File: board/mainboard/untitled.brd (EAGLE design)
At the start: 90 x 61 mm, 25 parts

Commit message: add catch sensor
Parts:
- added Q5: (no value), adafruit:SOT23
- added R11, R12: (no value), generic:SMD1608
- added X1: JST-XH-03-PIN-ROUND-PAD, Rembrandt Electronics - JST XH Connectors v1-0:JST-XH-03-PACKAGE-ROUND-PAD
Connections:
- new net CATCH_1: Q5.2, R12.2
- new net N$9: Q5.3, R11.2, X1.3
- net +3V3: now also Q5.1, R12.1
- net +5V: now also R11.1, X1.1
- net GND: now also X1.2
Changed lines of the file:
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@@
 <attribute name="VALUE" x="-45.25" y="-61.34" size="1.016" layer="27"/>
+</element>
+<element name="X1" library="Rembrandt Electronics - JST XH Connectors v1-0" package="JST-XH-03-PACKAGE-ROUND-PAD" value="JST-XH-03-PIN-ROUND-PAD" x="-38.1" y="-67.31" smashed="yes">
+<attribute name="NAME" x="-43.655" y="-69.35" size="1.016" layer="25" ratio="10" rot="R90"/>
+<attribute name="VALUE" x="-42.7025" y="-63.4175" size="1.016" layer="27" ratio="10"/>
+</element>
+<element name="Q5" library="adafruit" package="SOT23" value="" x="-43.18" y="-73.66" smashed="yes">
+<attribute name="NAME" x="-45.085" y="-71.755" size="1.27" layer="25"/>
+<attribute name="VALUE" x="-45.085" y="-76.835" size="1.27" layer="27"/>
+</element>
+<element name="R11" library="generic" package="SMD1608" value="" x="-40.64" y="-78.74" smashed="yes">
+<attribute name="NAME" x="-41.44" y="-78.09" size="1.016" layer="25"/>
+<attribute name="VALUE" x="-41.44" y="-80.39" size="1.016" layer="27"/>
+</element>
+<element name="R12" library="generic" package="SMD1608" value="" x="-44.45" y="-78.74" smashed="yes">
+<attribute name="NAME" x="-45.25" y="-78.09" size="1.016" layer="25"/>
+<attribute name="VALUE" x="-45.25" y="-80.39" size="1.016" layer="27"/>
 </element>
 </elements>
@@
 <contactref element="IR" pad="7"/>
 <contactref element="IR1" pad="7"/>
+<contactref element="X1" pad="2"/>
+<wire x1="-27.94" y1="-55.88" x2="-38.1" y2="-67.31" width="0" layer="19" extent="1-1"/>
 <wire x1="-12.065" y1="-16.115" x2="-27.94" y2="-55.88" width="0" layer="19" extent="1-1"/>
 <wire x1="-2.54" y1="-13.97" x2="-12.065" y2="-16.115" width="0" layer="19" extent="1-1"/>
@@
 <contactref element="R7" pad="1"/>
 <contactref element="R9" pad="1"/>
+<contactref element="X1" pad="1"/>
+<contactref element="R11" pad="1"/>
+<wire x1="-40.64" y1="-67.31" x2="-41.515" y2="-78.74" width="0" layer="19" extent="1-1"/>
+<wire x1="-41.515" y1="-59.69" x2="-40.64" y2="-67.31" width="0" layer="19" extent="1-1"/>
 <wire x1="-33.895" y1="-59.69" x2="-41.515" y2="-59.69" width="0" layer="19" extent="1-1"/>
 <wire x1="-25.4" y1="-55.88" x2="-33.895" y2="-59.69" width="0" layer="19" extent="1-1"/>
@@
 <contactref element="R10" pad="1"/>
 <contactref element="Q4" pad="1"/>
+<contactref element="R12" pad="1"/>
+<contactref element="Q5" pad="1"/>
+<wire x1="-44.13" y1="-74.76" x2="-45.325" y2="-78.74" width="0" layer="19" extent="1-1"/>
+<wire x1="-45.325" y1="-59.69" x2="-44.13" y2="-74.76" width="0" layer="19" extent="1-1"/>
 <wire x1="-37.705" y1="-59.69" x2="-45.325" y2="-59.69" width="0" layer="19" extent="1-1"/>
 <wire x1="-44.13" y1="-50.63" x2="-45.325" y2="-59.69" width="0" layer="19" extent="1-1"/>
@@
 <wire x1="-37.15" y1="-50.63" x2="-43.575" y2="-59.69" width="0" layer="19" extent="1-1"/>
 </signal>
+<signal name="N$9">
+<contactref element="X1" pad="3"/>
+<contactref element="Q5" pad="3"/>
+<contactref element="R11" pad="2"/>
+<wire x1="-43.18" y1="-72.56" x2="-39.765" y2="-78.74" width="0" layer="19" extent="1-1"/>
+<wire x1="-35.56" y1="-67.31" x2="-43.18" y2="-72.56" width="0" layer="19" extent="1-1"/>
+</signal>
+<signal name="CATCH_1">
+<contactref element="R12" pad="2"/>
+<contactref element="Q5" pad="2"/>
+<wire x1="-42.23" y1="-74.76" x2="-43.575" y2="-78.74" width="0" layer="19" extent="1-1"/>
+</signal>
 </signals>

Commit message: なんか
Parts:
- added JP1, JP2, JP3, JP4: (no value), pinhead:1X04
- added Q6: (no value), adafruit:SOT23
- added R13, R14: (no value), generic:SMD1608
- added X2: JST-XH-04-PIN-ROUND-PAD, Rembrandt Electronics - JST XH Connectors v1-0:JST-XH-04-PACKAGE-ROUND-PAD
- added X3: JST-XH-02-PIN-ROUND-PAD, Rembrandt Electronics - JST XH Connectors v1-0:JST-XH-02-PACKAGE-ROUND-PAD
- moved Q5 150.1 mm to (17.8, 63.5)
- moved R11 150.1 mm to (20.3, 58.4)
- moved R12 150.1 mm to (16.5, 58.4)
- moved X1 123.0 mm to (33.0, 33.0), turned to 270 degrees
- moved IR1 39.4 mm to (-24.1, -17.8)
- moved C2 0.38 mm to (-11.7, -15.2)
- moved R2 0.38 mm to (-9.78, -15.2)
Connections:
- new net CATCH_2: Q6.2, R14.2
- new net N$10: JP2.4, JP4.2
- new net N$11: JP2.3, JP4.3
- new net N$7: Q6.3, R13.2, X2.3
- new net N$8: X2.1, X3.2
- new net USB_D+: JP3.3
- new net USB_D-: JP3.4
- net +3V3: now also Q6.1, R14.1
- net +5V: now also R13.1, X2.4, X3.1
- net GND: now also JP3.1, JP4.4, X2.2
- net GYRO_D+: now also JP1.1
- net GYRO_D-: now also JP1.2
- net IR_D+: now also JP2.1
- net IR_D-: now also JP2.2
- net UVCC: now also JP3.2, JP4.1
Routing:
- net N$8: track 0.00 -> 147.8 mm
- net IR_D+: track 0.00 -> 30.3 mm
- net IR_D-: track 0.00 -> 26.7 mm
- net GYRO_D+: track 0.00 -> 25.2 mm
- net GYRO_D-: track 0.00 -> 23.7 mm, vias 0 -> 2
- net LINE_S22: track 26.1 -> 27.0 mm
- net LINE_S23: track 33.7 -> 34.3 mm
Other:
- outline, holes or cut-outs redrawn

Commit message: 作業PCの変更
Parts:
- added JP6: (no value), pinhead:2X07
- added X4: JST-XH-02-PIN-ROUND-PAD, Rembrandt Electronics - JST XH Connectors v1-0:JST-XH-02-PACKAGE-ROUND-PAD
- moved Q5 34.5 mm to (27.9, 30.5), turned to 270 degrees
- moved R12 29.0 mm to (24.1, 30.5), turned to 270 degrees
- moved R11 25.3 mm to (29.1, 34.7), turned to 270 degrees
- moved R13 20.5 mm to (29.2, 26.7), turned to 270 degrees
- moved R14 19.4 mm to (21.6, 26.7), turned to 270 degrees
- moved Q6 19.3 mm to (25.4, 26.7), turned to 270 degrees
- moved X2 2.54 mm to (40.6, 29.2)
- moved X3 2.54 mm to (-40.6, 31.8)
- moved MD1 1.27 mm to (35.6, 12.1), flipped to the bottom
- moved MD3 1.27 mm to (-35.6, 12.1), flipped to the bottom
- moved MD2 1.27 mm to (41.9, 12.1), flipped to the bottom
- moved MD4 1.27 mm to (-41.9, 12.1), flipped to the bottom
- moved JP3 0.64 mm to (-39.4, -15.9)
- moved JP1 0.64 mm to (-43.2, 0.64)
- moved JP2 0.64 mm to (-35.6, 0.64)
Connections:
- new net KICK: U$1.P$9, X4.2
- net GND: now also X4.1
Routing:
- net +5V: track 0.00 -> 54.8 mm, vias 0 -> 1
- net N$11: track 0.00 -> 47.3 mm
- net N$10: track 0.00 -> 47.3 mm
- net MD2_TX: track 0.00 -> 36.3 mm
- net N$8: track 147.8 -> 112.0 mm
- net MD2_RX: track 0.00 -> 30.9 mm
- net GND: track 0.00 -> 20.7 mm
- net N$7: track 0.00 -> 16.4 mm
- net MD1_TX: track 0.00 -> 15.8 mm, vias 0 -> 1
- net N$9: track 0.00 -> 7.29 mm
- net MD1_RX: track 0.00 -> 6.40 mm
- net +3V3: track 0.00 -> 5.48 mm
- net CATCH_2: track 0.00 -> 2.74 mm
- net CATCH_1: track 0.00 -> 2.74 mm
- net GYRO_D+: track 25.2 -> 25.8 mm
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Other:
- outline, holes or cut-outs redrawn

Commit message: complete mainboard
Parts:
- removed JP6: (no value), pinhead:2X07
- added JP5: (no value), pinhead:2X06
- added X5: JST-XH-02-PIN-ROUND-PAD, Rembrandt Electronics - JST XH Connectors v1-0:JST-XH-02-PACKAGE-ROUND-PAD
- moved R5 58.9 mm to (-1.27, -4.45), turned to 180 degrees
- moved R10 54.1 mm to (-34.9, -6.48), flipped to the bottom, turned to 180 degrees
- moved R8 53.4 mm to (-38.7, -6.35), flipped to the bottom, turned to 180 degrees
- moved R3 51.4 mm to (-1.27, -2.54), turned to 180 degrees
- moved Q2 49.9 mm to (-6.99, -5.08), turned to 270 degrees
- moved R6 49.8 mm to (-10.2, -5.08), turned to 270 degrees
- moved R7 48.6 mm to (-25.4, -13.6), turned to 180 degrees
- moved R4 47.2 mm to (-10.2, -1.91), turned to 270 degrees
- moved R9 45.1 mm to (-25.4, -15.2), turned to 180 degrees
- moved Q1 43.2 mm to (-6.99, -1.91), turned to 270 degrees
- moved Q3 40.3 mm to (-38.7, -9.53), flipped to the bottom, turned to 180 degrees
- moved Q4 40.1 mm to (-34.9, -9.53), flipped to the bottom, turned to 180 degrees
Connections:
- new net LED1: JP5.4, U$1.P$20
- new net LED2: JP5.6, U$1.P$21
- new net LED3: JP5.5, U$1.P$5
- new net LED4: JP5.7, U$1.P$6
- new net LED5: JP5.8, U$1.P$9
- new net LED6: JP5.10, U$1.P$37
- new net MAIN_RESET: JP5.11, U$1.P$40
- new net RASPI_RESET: JP5.12, RASPI.5
- new net SWITCH: JP5.3, U$1.P$45
- net +5V: now also X5.2
- net GND: now also JP5.2, X5.1
- net GYRO_RESET: now also JP5.1
- net GYRO_RX: now also U$1.P$33
- net GYRO_TX: now also U$1.P$32
- net IR_RESET: now also JP5.9
- net KICK: now also U$1.P$10; no longer U$1.P$9
- net MD3_RX: now also U$1.P$15; no longer U$1.P$28
- net MD3_TX: now also U$1.P$16; no longer U$1.P$29
- net MD4_RX: now also U$1.P$28; no longer U$1.P$33
- net MD4_TX: now also U$1.P$29; no longer U$1.P$32
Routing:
- net GND: track 20.7 -> 240.9 mm, vias 0 -> 3
- net +5V: track 54.8 -> 269.7 mm, vias 1 -> 8
- net +3V3: track 5.48 -> 149.4 mm, vias 0 -> 10
- net UVCC: track 0.00 -> 82.5 mm, vias 0 -> 3
- net LED6: track 0.00 -> 80.6 mm, vias 0 -> 3
- net RASPI_RESET: track 0.00 -> 78.3 mm, vias 0 -> 4
- net MAIN_RESET: track 0.00 -> 77.9 mm, vias 0 -> 3
- net MD3_RX: track 0.00 -> 63.2 mm, vias 0 -> 1
- net MD3_TX: track 0.00 -> 61.0 mm, vias 0 -> 2
- net MD4_RX: track 0.00 -> 54.8 mm
- net MD4_TX: track 0.00 -> 47.5 mm
- net SWITCH: track 0.00 -> 47.2 mm, vias 0 -> 1
- net GYRO_RESET: track 0.00 -> 46.8 mm
- net IR_RESET: track 0.00 -> 44.4 mm
- net LED4: track 0.00 -> 33.4 mm, vias 0 -> 1
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
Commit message: marge前のファイル
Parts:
- removed JP5: (no value), pinhead:2X06
- added JP7: (no value), pinhead:2X07
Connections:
- new net TRIM: JP7.14, U$1.P$44
- net +3V3: now also JP7.13
- net GND: now also JP7.2; no longer JP5.2
- net GYRO_RESET: now also JP7.1; no longer JP5.1
- net IR_RESET: now also JP7.9; no longer JP5.9
- net LED1: now also JP7.4; no longer JP5.4
- net LED2: now also JP7.6; no longer JP5.6
- net LED3: now also JP7.5; no longer JP5.5
- net LED4: now also JP7.7; no longer JP5.7
- net LED5: now also JP7.8; no longer JP5.8
- net LED6: now also JP7.10; no longer JP5.10
- net MAIN_RESET: now also JP7.11; no longer JP5.11
- net RASPI_RESET: now also JP7.12; no longer JP5.12
- net SWITCH: now also JP7.3; no longer JP5.3
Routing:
- net TRIM: track 0.00 -> 65.2 mm, vias 0 -> 2
- net +3V3: track 149.4 -> 174.7 mm

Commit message: Revert "Merge remote-tracking branch 'origin/Develop' into feature_#37"
This reverts commit cb103155361e8766478c6830db153463370c0739, reversing
changes made to 84e093fe944e1f8653a6822ff34e6f8740617cb5.
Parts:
- removed JP7: (no value), pinhead:2X07
- added JP5: (no value), pinhead:2X06
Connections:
- removed net TRIM: JP7.14, U$1.P$44
- net +3V3: no longer JP7.13
- net GND: now also JP5.2; no longer JP7.2
- net GYRO_RESET: now also JP5.1; no longer JP7.1
- net IR_RESET: now also JP5.9; no longer JP7.9
- net LED1: now also JP5.4; no longer JP7.4
- net LED2: now also JP5.6; no longer JP7.6
- net LED3: now also JP5.5; no longer JP7.5
- net LED4: now also JP5.7; no longer JP7.7
- net LED5: now also JP5.8; no longer JP7.8
- net LED6: now also JP5.10; no longer JP7.10
- net MAIN_RESET: now also JP5.11; no longer JP7.11
- net RASPI_RESET: now also JP5.12; no longer JP7.12
- net SWITCH: now also JP5.3; no longer JP7.3
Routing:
- net TRIM: track 65.2 -> 0.00 mm, vias 2 -> 0
- net +3V3: track 174.7 -> 149.4 mm

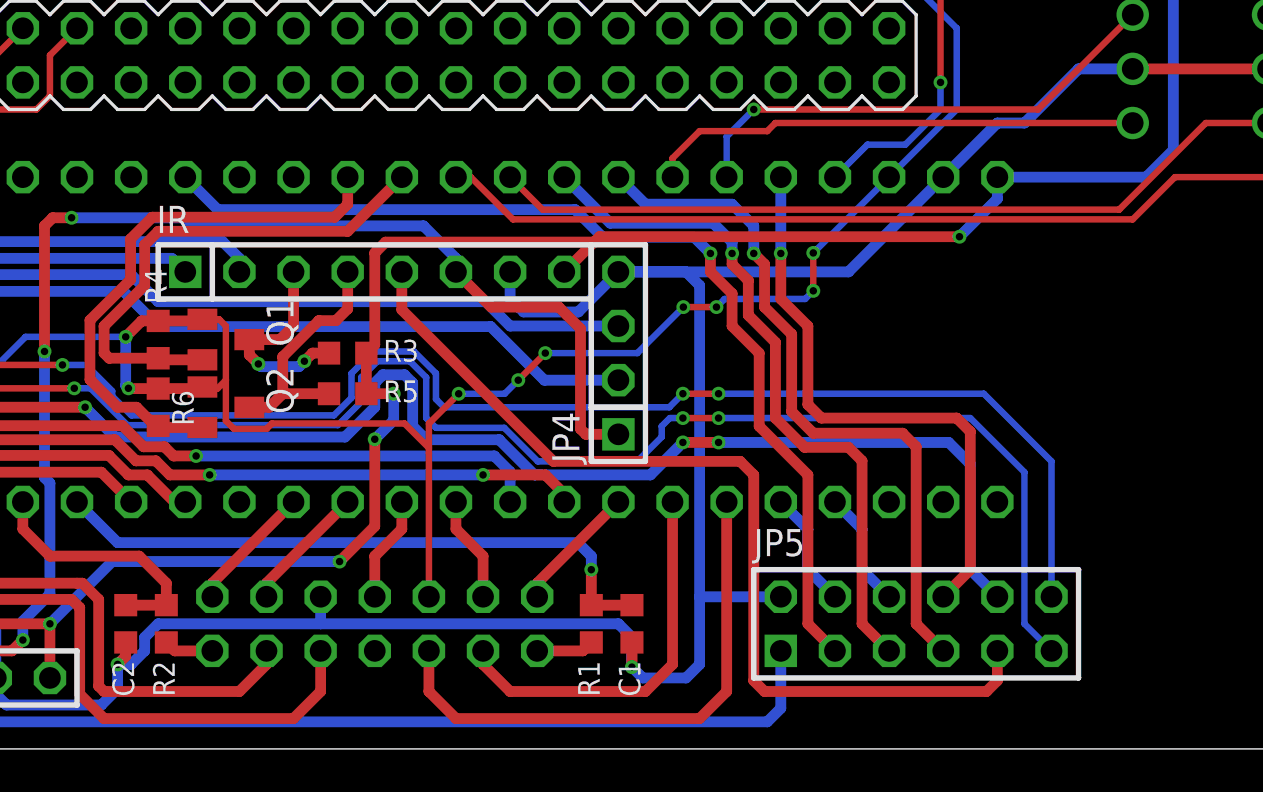
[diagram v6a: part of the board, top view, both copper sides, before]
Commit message: 可変抵抗の追加
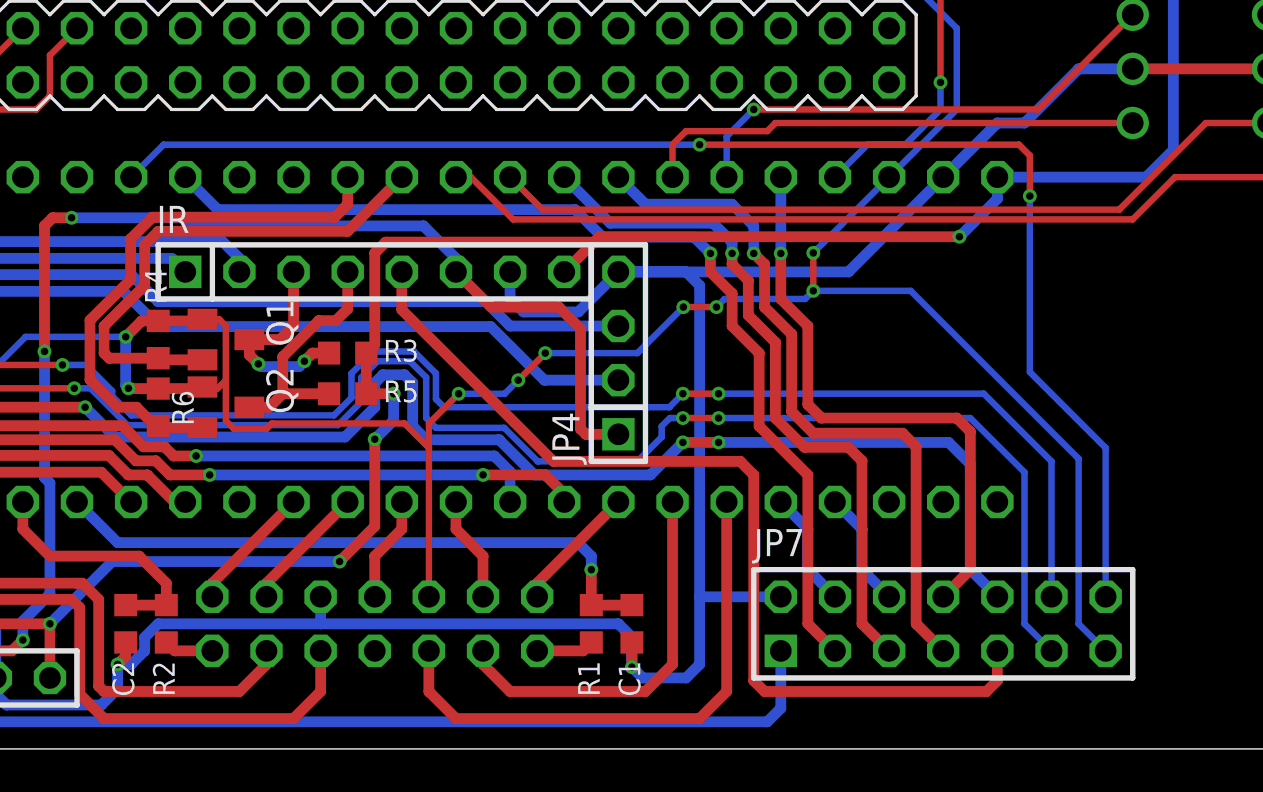
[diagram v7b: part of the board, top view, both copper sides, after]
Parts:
- removed JP5: (no value), pinhead:2X06
- added JP7: (no value), pinhead:2X07
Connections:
- new net TRIM: JP7.14, U$1.P$44
- net +3V3: now also JP7.13
- net GND: now also JP7.2; no longer JP5.2
- net GYRO_RESET: now also JP7.1; no longer JP5.1
- net IR_RESET: now also JP7.9; no longer JP5.9
- net LED1: now also JP7.4; no longer JP5.4
- net LED2: now also JP7.6; no longer JP5.6
- net LED3: now also JP7.5; no longer JP5.5
- net LED4: now also JP7.7; no longer JP5.7
- net LED5: now also JP7.8; no longer JP5.8
- net LED6: now also JP7.10; no longer JP5.10
- net MAIN_RESET: now also JP7.11; no longer JP5.11
- net RASPI_RESET: now also JP7.12; no longer JP5.12
- net SWITCH: now also JP7.3; no longer JP5.3
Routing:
- net TRIM: track 0.00 -> 65.2 mm, vias 0 -> 2
- net +3V3: track 149.4 -> 174.7 mm
